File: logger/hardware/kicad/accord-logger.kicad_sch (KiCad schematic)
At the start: 153 parts, among them J1 Board connector 14-way, J3 Spare GP13 / switched power, J4 Reset RUN-GND, J5 SD breakout 6-way, Q1 MMBT3904, Q2 BSS138P, Q3 BSS138P, Q4 BSS138P, Q5 IPD50P04P4L-11, Q6 2N3904, Q7 2N3904, Q8 BSS138P, Q9 MMBT3904, U1 RaspberryPi_Pico_W, U10 CD74HC4060M96, U11 CD74HC4020M96, U12 CD4011BM96, U13 CD4071BM96, U14 CD4093BM96, U15 MAX3485, U16 DS3231SN, U2 PC817, U3 ASSR-601JV, U4 TPS70950QDBVRQ1, U5 TPS3839K50DBZR, U6 LM2678T-5.0, U7 OV-7604-C7-32.768KHZ-20PPM-TA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, U8 74AHC1G17GV, U9 SN74LVC1G97DBVR

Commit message: schematic: J3 becomes a 2x03 carrying GP11 and GP12 (D-HDR-16)
Owner: "I removed GP12 and GP11 test points, would prefer to change J3 to
a 6 pin header, either 1x06 or 2x03", then "2x03 please". J3 goes from
Conn_01x04 / PinHeader_1x04 to Conn_02x03_Odd_Even /
PinHeader_2x03_P2.54mm_Vertical: 1 B5, 2 PGND, 3 P3V3_SW, 4 SPARE_GP13
(unchanged), 5 SPARE_GP12, 6 SPARE_GP11. TP24/TP25 and their label stubs
are removed; BOM.csv, check_capture.py (new 2x03 check) and the
`headers` step follow. A 1x06 was ruled out on the board: extended down
it reaches H4 and the antenna strip, extended up it meets R21.

ERC 0; full-netlist capture 783/783; reference pin map refreshed after
confirming only J3.5, J3.6, TP24.1 and TP25.1 moved; closure 67/67; 151
BOM rows; courtyard allowance 1.62x. DRC parity against the board now
differs only at J3, until the owner runs Update PCB from Schematic.
STATUS rewritten to the current step (phase D next).

Claude-Session-ID: d2c32eb9-406b-48d8-b5b5-bb1d8d4746af
Co-Authored-By: Claude Opus 5.5 <noreply@anthropic.com>
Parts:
- removed TP24, TP25: TestPoint, TestPoint:TestPoint_Pad_D2.0mm, symbol Connector:TestPoint
- J3: value Spare GP13 / switched power -> Spare GP11-13 / switched power; footprint Connector_PinHeader_2.54mm:PinHeader_1x04_P2.54mm_Vertical -> Connector_PinHeader_2.54mm:PinHeader_2x03_P2.54mm_Vertical; symbol Connector_Generic:Conn_01x04 -> Connector_Generic:Conn_02x03_Odd_Even
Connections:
- net SPARE_GP11: now also J3.6 (Pin_6)
- net SPARE_GP12: now also J3.5 (Pin_5)

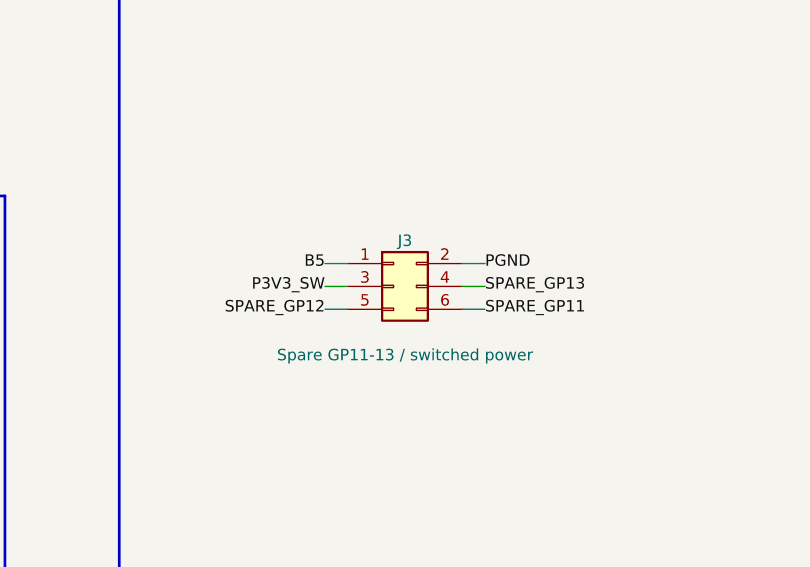
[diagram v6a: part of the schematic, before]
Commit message: schematic: J3 pins 3 and 4 swapped to match the owner's routing
Owner: "keep my routing, I swapped the GP13 and 3v3 pins for ease of
routing". J3 is now 1 B5, 2 PGND, 3 SPARE_GP13, 4 P3V3_SW, 5 SPARE_GP12,
6 SPARE_GP11 (two labels swapped). check_capture.py, BOM.csv, STATUS and
DECISIONS D-HDR-16 follow.

ERC 0; full-netlist capture 783/783; reference pin map refreshed after
confirming only J3.3 and J3.4 moved; closure 67/67; DRC schematic parity
0 against the board.

Claude-Session-ID: d2c32eb9-406b-48d8-b5b5-bb1d8d4746af
Co-Authored-By: Claude Opus 5.5 <noreply@anthropic.com>
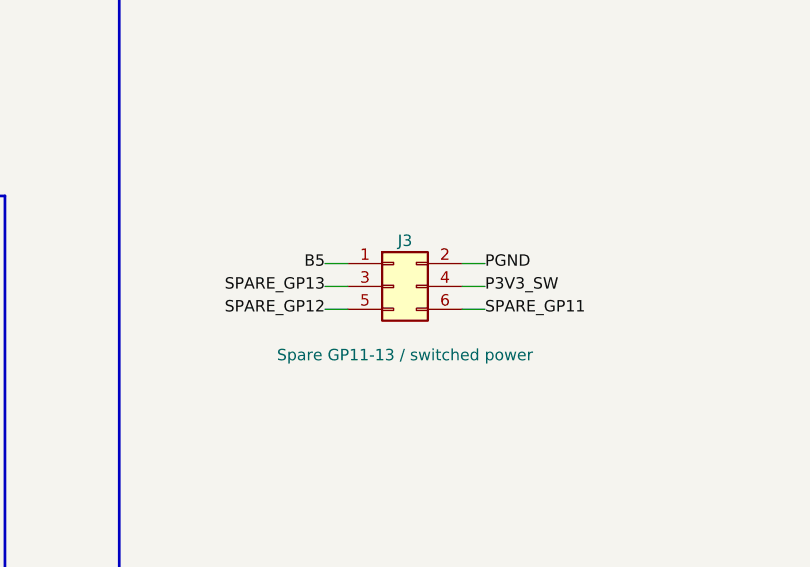
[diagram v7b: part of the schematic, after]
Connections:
- net P3V3_SW: now also J3.4 (Pin_4); no longer J3.3 (Pin_3)
- net SPARE_GP13: now also J3.3 (Pin_3); no longer J3.4 (Pin_4)
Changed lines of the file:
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@@
 		)
 	)
-	(label "P3V3_SW"
+	(label "SPARE_GP13"
 		(at 396.24 480.06 180)
 		(effects
@@
 		)
 	)
-	(label "SPARE_GP13"
+	(label "P3V3_SW"
 		(at 414.02 480.06 0)
 		(effects
